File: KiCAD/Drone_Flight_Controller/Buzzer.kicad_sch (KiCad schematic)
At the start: 4 parts, among them Q2 2SC1815

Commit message: Add Components to BOM
Add Components to BOM
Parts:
- R10: footprint (none) -> Resistor_SMD:R_0805_2012Metric_Pad1.20x1.40mm_HandSolder; Link (none) -> https://www.mouser.at/ProductDetail/Panasonic/ERA-6AEB181V?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
- R9: footprint (none) -> Resistor_SMD:R_0805_2012Metric_Pad1.20x1.40mm_HandSolder; Link (none) -> https://www.mouser.at/ProductDetail/Susumu/RG2012P-102-B-T5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
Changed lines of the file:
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@@
 			)
 		)
-		(property "Footprint" ""
+		(property "Footprint" "Resistor_SMD:R_0805_2012Metric_Pad1.20x1.40mm_HandSolder"
 			(at 106.68 107.188 90)
 			(effects
@@
 			)
 		)
-		(property "Datasheet" "~"
+		(property "Datasheet" "https://industrial.panasonic.com/cdbs/www-data/pdf/RDM0000/AOA0000C307.pdf"
 			(at 106.68 105.41 0)
 			(effects
@@
 		(property "Description" "Resistor"
 			(at 106.68 105.41 0)
+			(effects
+				(font
+					(size 1.27 1.27)
+				)
+				(hide yes)
+			)
+		)
+		(property "Link" "https://www.mouser.at/ProductDetail/Panasonic/ERA-6AEB181V?qs=sGAEpiMZZMtlubZbdhIBIK8nywws5AKnTCAIBrFldM0%3D"
+			(at 106.68 105.41 90)
 			(effects
 				(font
@@
 			)
 		)
-		(property "Footprint" ""
+		(property "Footprint" "Resistor_SMD:R_0805_2012Metric_Pad1.20x1.40mm_HandSolder"
 			(at 118.872 91.44 90)
 			(effects
@@
 			)
 		)
-		(property "Datasheet" "~"
+		(property "Datasheet" "https://www.mouser.at/datasheet/2/392/n_catalog_partition01_en-1140338.pdf"
 			(at 120.65 91.44 0)
 			(effects
@@
 			(at 120.65 91.44 0)
 			(effects
+				(font
+					(size 1.27 1.27)
+				)
+				(hide yes)
+			)
+		)
+		(property "Link" "https://www.mouser.at/ProductDetail/Susumu/RG2012P-102-B-T5?qs=sGAEpiMZZMtlubZbdhIBIPbXU5%252BlCJyDoLLmdukvSY0%3D"
+			(at 120.65 91.44 0)
+			(effects

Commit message: Reanotate
Reanotate
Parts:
- renumbered BZ1 to BZ501, Q2 to Q501, R10 to R501, R9 to R502
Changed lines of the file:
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@@
 		(dnp no)
 		(fields_autoplaced yes)
-		(property "Reference" "R10"
+		(property "Reference" "R501"
 			(at 106.68 99.06 90)
 			(effects
@@
 			(project ""
 				(path "/05daaa24-e506-4b9a-9564-8bf799413ca8/be7f0ff9-fd1d-432b-97a6-9126ad5ddcf4"
-					(reference "R10")
+					(reference "R501")
 					(unit 1)
 				)
@@
 		(dnp no)
 		(fields_autoplaced yes)
-		(property "Reference" "BZ1"
+		(property "Reference" "BZ501"
 			(at 135.89 90.1699 0)
 			(effects
@@
 			(project "Drone_Flight_Controller"
 				(path "/05daaa24-e506-4b9a-9564-8bf799413ca8/be7f0ff9-fd1d-432b-97a6-9126ad5ddcf4"
-					(reference "BZ1")
+					(reference "BZ501")
 					(unit 1)
 				)
@@
 		(dnp no)
 		(fields_autoplaced yes)
-		(property "Reference" "#PWR010"
+		(property "Reference" "#PWR0501"
 			(at 120.65 86.36 0)
 			(effects
@@
 			(project ""
 				(path "/05daaa24-e506-4b9a-9564-8bf799413ca8/be7f0ff9-fd1d-432b-97a6-9126ad5ddcf4"
-					(reference "#PWR010")
+					(reference "#PWR0501")
 					(unit 1)
 				)
@@
 		(dnp no)
 		(fields_autoplaced yes)
-		(property "Reference" "R9"
+		(property "Reference" "R502"
 			(at 123.19 90.1699 0)
 			(effects
@@
 			(project ""
 				(path "/05daaa24-e506-4b9a-9564-8bf799413ca8/be7f0ff9-fd1d-432b-97a6-9126ad5ddcf4"
-					(reference "R9")
+					(reference "R502")
 					(unit 1)
 				)
@@
 		(dnp no)
 		(fields_autoplaced yes)
-		(property "Reference" "#PWR011"
+		(property "Reference" "#PWR0502"
 			(at 120.65 119.38 0)
 			(effects
@@
 			(project ""
 				(path "/05daaa24-e506-4b9a-9564-8bf799413ca8/be7f0ff9-fd1d-432b-97a6-9126ad5ddcf4"
-					(reference "#PWR011")
+					(reference "#PWR0502")
 					(unit 1)
 				)
@@
 		(dnp no)
 		(fields_autoplaced yes)
-		(property "Reference" "Q2"
+		(property "Reference" "Q501"
 			(at 123.19 104.1399 0)
 			(effects
@@
 			(project ""
 				(path "/05daaa24-e506-4b9a-9564-8bf799413ca8/be7f0ff9-fd1d-432b-97a6-9126ad5ddcf4"
-					(reference "Q2")
-					(unit 1)
-				)
+					(reference "Q501")
+					(unit 1)
+				)

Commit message: Reannotate
Reannotate
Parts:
- renumbered R502 to R501, R501 to R502
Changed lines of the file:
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@@
 		(dnp no)
 		(fields_autoplaced yes)
-		(property "Reference" "R501"
+		(property "Reference" "R502"
 			(at 106.68 99.06 90)
 			(effects
@@
 			(project ""
 				(path "/05daaa24-e506-4b9a-9564-8bf799413ca8/be7f0ff9-fd1d-432b-97a6-9126ad5ddcf4"
-					(reference "R501")
+					(reference "R502")
 					(unit 1)
 				)
@@
 		(dnp no)
 		(fields_autoplaced yes)
-		(property "Reference" "R502"
+		(property "Reference" "R501"
 			(at 123.19 90.1699 0)
 			(effects
@@
 			(project ""
 				(path "/05daaa24-e506-4b9a-9564-8bf799413ca8/be7f0ff9-fd1d-432b-97a6-9126ad5ddcf4"
-					(reference "R502")
-					(unit 1)
-				)
+					(reference "R501")
+					(unit 1)
+				)

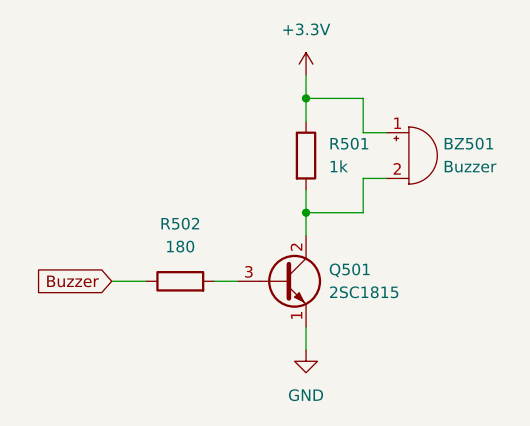
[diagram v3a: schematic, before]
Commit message: Change Transistors to SMD Variants
Change Transistors to SMD Variants
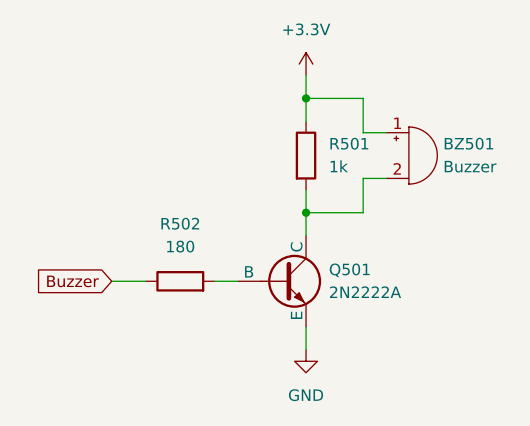
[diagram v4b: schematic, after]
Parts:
- removed Q501: 2SC1815, Package_TO_SOT_THT:TO-92_Inline, symbol Transistor_BJT:2SC1815
- added Q501: 2N2222A, Package_TO_SOT_THT:TO-92_HandSolder, symbol Simulation_SPICE:NPN
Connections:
- net GND: now also Q501.3 (E)
- net at R502.2: now also Q501.2 (B)
- net at BZ501.2 (-), R501.2: now also Q501.1 (C)
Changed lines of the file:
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@@
+	)
+	(symbol
+		(lib_id "Simulation_SPICE:NPN")
+		(at 118.11 105.41 0)
+		(unit 1)
+		(exclude_from_sim no)
+		(in_bom yes)
+		(on_board yes)
+		(dnp no)
+		(fields_autoplaced yes)
+		(property "Reference" "Q501"
+			(at 123.19 104.1399 0)
+			(effects
+				(font
+					(size 1.27 1.27)
+				)
+				(justify left)
+			)
+		)
+		(property "Value" "2N2222A"
+			(at 123.19 106.6799 0)
+			(effects
+				(font
+					(size 1.27 1.27)
+				)
+				(justify left)
+			)
+		)
+		(property "Footprint" "Package_TO_SOT_THT:TO-92_HandSolder"
+			(at 181.61 105.41 0)
+			(effects
+				(font
+					(size 1.27 1.27)
+				)
+				(hide yes)
+			)
+		)
+		(property "Datasheet" "https://diotec.com/request/datasheet/2n2222a.pdf"
+			(at 181.61 105.41 0)
+			(effects
+				(font
+					(size 1.27 1.27)
+				)
+				(hide yes)
+			)
+		)
+		(property "Description" "Bipolar transistor symbol for simulation only, substrate tied to the emitter"
+			(at 118.11 105.41 0)
+			(effects
+				(font
+					(size 1.27 1.27)
+				)
+				(hide yes)
+			)
+		)
+		(property "Sim.Device" "NPN"
+			(at 118.11 105.41 0)
+			(effects
+				(font
+					(size 1.27 1.27)
+				)
+				(hide yes)
+			)
+		)
+		(property "Sim.Type" "GUMMELPOON"
+			(at 118.11 105.41 0)
+			(effects
+				(font
+					(size 1.27 1.27)
+				)
+				(hide yes)
+			)
+		)
+		(property "Sim.Pins" "1=C 2=B 3=E"
+			(at 118.11 105.41 0)
+			(effects
+				(font
+					(size 1.27 1.27)
+				)
+				(hide yes)
+			)
+		)
+		(property "Link" "https://www.mouser.at/ProductDetail/Diotec-Semiconductor/2N2222A?qs=OlC7AqGiEDmNlRSTGL2dYg%3D%3D"
+			(at 118.11 105.41 0)
+			(effects
+				(font
+					(size 1.27 1.27)
+				)
+				(hide yes)
+			)
+		)
+		(pin "1"
+		)
+		(pin "2"
+		)
+		(pin "3"
+		)
+		(instances
+			(project ""
+				(path "/05daaa24-e506-4b9a-9564-8bf799413ca8/be7f0ff9-fd1d-432b-97a6-9126ad5ddcf4"
+					(reference "Q501")
+					(unit 1)
+				)
+			)
+		)
 	)
 	(symbol
@@
 					(unit 1)
 				)
-			)
-		)
-	)
-	(symbol
-		(lib_id "Transistor_BJT:2SC1815")
-		(at 118.11 105.41 0)
-		(unit 1)
-		(exclude_from_sim no)
-		(in_bom yes)
-		(on_board yes)
-		(dnp no)
-		(fields_autoplaced yes)
-		(property "Reference" "Q501"
-			(at 123.19 104.1399 0)
-			(effects
-				(font
-					(size 1.27 1.27)
-				)
-				(justify left)
-			)
-		)
-		(property "Value" "2SC1815"
-			(at 123.19 106.6799 0)
-			(effects
-				(font
-					(size 1.27 1.27)
-				)
-				(justify left)
-			)
-		)
-		(property "Footprint" "Package_TO_SOT_THT:TO-92_Inline"
-			(at 123.19 107.315 0)
-			(effects
-				(font
-					(size 1.27 1.27)
-					(italic yes)
-				)
-				(justify left)
-				(hide yes)
-			)
-		)
-		(property "Datasheet" "https://media.digikey.com/pdf/Data%20Sheets/Toshiba%20PDFs/2SC1815.pdf"
-			(at 118.11 105.41 0)
-			(effects
-				(font
-					(size 1.27 1.27)
-				)
-				(justify left)
-				(hide yes)
-			)
-		)
-		(property "Description" "0.15A Ic, 50V Vce, Low Noise Audio NPN Transistor, TO-92"
-			(at 118.11 105.41 0)
-			(effects
-				(font
-					(size 1.27 1.27)
-				)
-				(hide yes)
-			)
-		)
-		(pin "1"
-		)
-		(pin "3"
-		)
-		(pin "2"
-		)
-		(instances
-			(project ""
-				(path "/05daaa24-e506-4b9a-9564-8bf799413ca8/be7f0ff9-fd1d-432b-97a6-9126ad5ddcf4"
-					(reference "Q501")
-					(unit 1)
-				)

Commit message: Reannotate
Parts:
- renumbered BZ501 to BZ401, Q501 to Q401, R501 to R401, R502 to R402
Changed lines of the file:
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@@
 		(dnp no)
 		(fields_autoplaced yes)
-		(property "Reference" "R502"
+		(property "Reference" "R402"
 			(at 106.68 99.06 90)
 			(effects
@@
 			(project ""
 				(path "/05daaa24-e506-4b9a-9564-8bf799413ca8/be7f0ff9-fd1d-432b-97a6-9126ad5ddcf4"
-					(reference "R502")
+					(reference "R402")
 					(unit 1)
 				)
@@
 		(dnp no)
 		(fields_autoplaced yes)
-		(property "Reference" "BZ501"
+		(property "Reference" "BZ401"
 			(at 135.89 90.1699 0)
 			(effects
@@
 			(project "Drone_Flight_Controller"
 				(path "/05daaa24-e506-4b9a-9564-8bf799413ca8/be7f0ff9-fd1d-432b-97a6-9126ad5ddcf4"
-					(reference "BZ501")
+					(reference "BZ401")
 					(unit 1)
 				)
@@
 		(dnp no)
 		(fields_autoplaced yes)
-		(property "Reference" "#PWR0501"
+		(property "Reference" "#PWR0401"
 			(at 120.65 86.36 0)
 			(effects
@@
 			(project ""
 				(path "/05daaa24-e506-4b9a-9564-8bf799413ca8/be7f0ff9-fd1d-432b-97a6-9126ad5ddcf4"
-					(reference "#PWR0501")
+					(reference "#PWR0401")
 					(unit 1)
 				)
@@
 		(dnp no)
 		(fields_autoplaced yes)
-		(property "Reference" "R501"
+		(property "Reference" "R401"
 			(at 123.19 90.1699 0)
 			(effects
@@
 			(project ""
 				(path "/05daaa24-e506-4b9a-9564-8bf799413ca8/be7f0ff9-fd1d-432b-97a6-9126ad5ddcf4"
-					(reference "R501")
+					(reference "R401")
 					(unit 1)
 				)
@@
 		(dnp no)
 		(fields_autoplaced yes)
-		(property "Reference" "Q501"
+		(property "Reference" "Q401"
 			(at 123.19 104.1399 0)
 			(effects
@@
 			(project ""
 				(path "/05daaa24-e506-4b9a-9564-8bf799413ca8/be7f0ff9-fd1d-432b-97a6-9126ad5ddcf4"
-					(reference "Q501")
+					(reference "Q401")
 					(unit 1)
 				)
@@
 		(dnp no)
 		(fields_autoplaced yes)
-		(property "Reference" "#PWR0502"
+		(property "Reference" "#PWR0402"
 			(at 120.65 119.38 0)
 			(effects
@@
 			(project ""
 				(path "/05daaa24-e506-4b9a-9564-8bf799413ca8/be7f0ff9-fd1d-432b-97a6-9126ad5ddcf4"
-					(reference "#PWR0502")
-					(unit 1)
-				)
+					(reference "#PWR0402")
+					(unit 1)
+				)

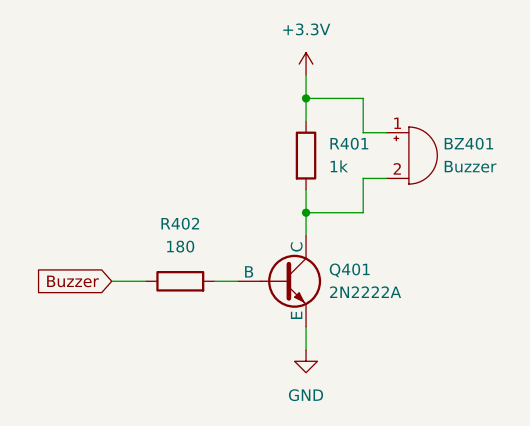
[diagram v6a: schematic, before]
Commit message: Change "+3.3V" to "+3V3" for consistency
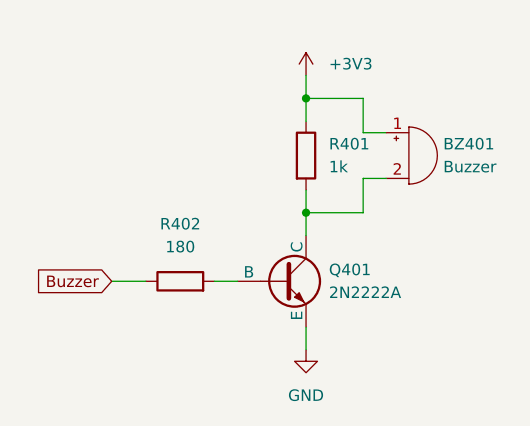
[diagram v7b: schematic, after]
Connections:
- net +3.3V renamed +3V3
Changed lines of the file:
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@@
 	(title_block
 		(title "Buzzer")
-		(date "2025-07-02")
-		(rev "V1")
+		(date "2025-09-19")
+		(rev "V2")
 		(company "HTL Steyr")
 		(comment 1 "Felix Brandner")
@@
 		(dnp no)
 		(fields_autoplaced yes)
-		(property "Reference" "#PWR0401"
+		(property "Reference" "+3V3"
 			(at 120.65 86.36 0)
 			(effects
@@
 			)
 		)
-		(property "Value" "+3.3V"
-			(at 120.65 77.47 0)
-			(effects
-				(font
-					(size 1.27 1.27)
-				)
+		(property "Value" "+3V3"
+			(at 123.19 81.2799 0)
+			(effects
+				(font
+					(size 1.27 1.27)
+				)
+				(justify left)
 			)
 		)
@@
 			(project ""
 				(path "/05daaa24-e506-4b9a-9564-8bf799413ca8/be7f0ff9-fd1d-432b-97a6-9126ad5ddcf4"
-					(reference "#PWR0401")
+					(reference "+3V3")
 					(unit 1)
 				)
